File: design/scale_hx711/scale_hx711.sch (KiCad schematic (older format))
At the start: 0 parts

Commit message: PCB Files added, for scale_hx711
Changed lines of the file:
@@
 F0 "nRF" 50
 F1 "nRF.sch" 50
+F2 "VBAT" O R 6450 3700 50
+F3 "HX711_DATA" I R 6450 4100 50
+F4 "HX711_RATE" O R 6450 4510 50
+F5 "HX711_CLK" B R 6450 4900 50
+F6 "BOOST_EN" O R 6450 5300 50
+F7 "10V_LDO_EN" O R 6450 2900 50
+F8 "Vlc" I R 6450 3300 50
+F9 "EINK_SDIO" O L 4400 3300 50
+F10 "EINK_SCLK" O L 4400 3700 50
+F11 "EINK_CS" O L 4400 4100 50
+F12 "EINK_RST" O L 4400 4510 50
+F13 "EINK_BUSY" I L 4400 4900 50
 $EndSheet
 $Sheet
@@
 F0 "Sheet5E60241E" 50
 F1 "epaper.sch" 50
+F2 "EINK_SDIO" I R 3800 3300 50
+F3 "EINK_SCLK" I R 3800 3700 50
+F4 "EINK_CS" I R 3800 4100 50
+F5 "EINK_RST" I R 3800 4510 50
+F6 "EINK_BUSY" O R 3800 4900 50
 $EndSheet
 $Sheet
@@
 F0 "Sheet5E602498" 50
 F1 "loadcell.sch" 50
+F2 "VBAT" I L 8550 3700 50
+F3 "HX711_RATE" I L 8550 4510 50
+F4 "HX711_DATA" O L 8550 4100 50
+F5 "HX711_CLK" B L 8550 4900 50
+F6 "BOOST_EN" I L 8550 5300 50
+F7 "10V_LDO_EN" I L 8550 2900 50
+F8 "Vlc" O L 8550 3300 50
 $EndSheet
+Wire Wire Line
+	3800 3300 4400 3300
+Wire Wire Line
+	4400 3700 3800 3700
+Wire Wire Line
+	3800 4100 4400 4100
+Wire Wire Line
+	3800 4510 4400 4510
+Wire Wire Line
+	4400 4900 3800 4900
+Wire Wire Line
+	6450 5300 8550 5300
+Wire Wire Line
+	8550 4900 6450 4900
+Wire Wire Line
+	6450 4510 8550 4510
+Wire Wire Line
+	8550 4100 6450 4100
+Wire Wire Line
+	6450 3700 8550 3700
+Wire Wire Line
+	8550 3300 6450 3300
+Wire Wire Line
+	6450 2900 8550 2900
 $EndSCHEMATC

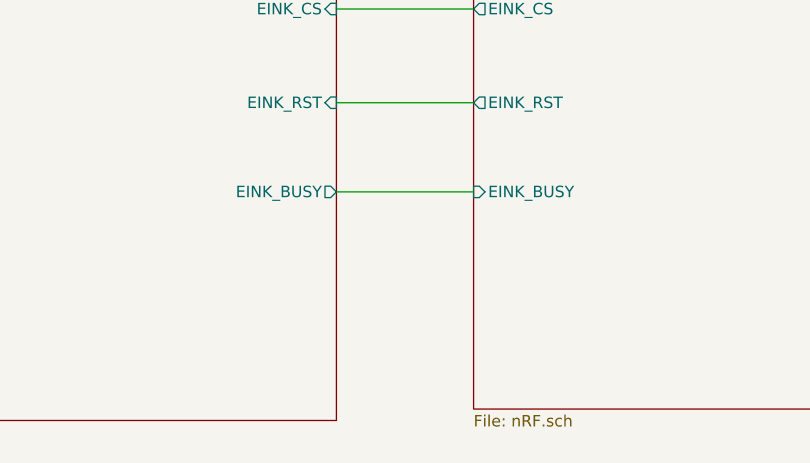
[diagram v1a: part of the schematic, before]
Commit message: DC, CS pins separated, issue fixed. In both scale_hx711 and scale_ltc6915.
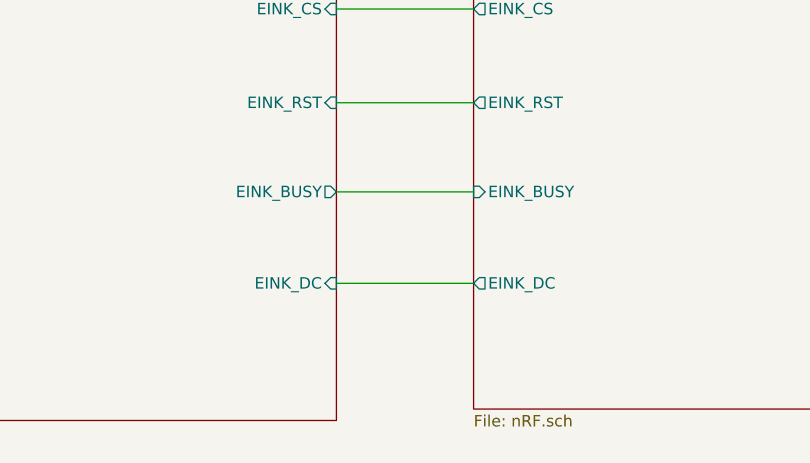
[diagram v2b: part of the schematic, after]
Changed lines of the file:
@@
 F12 "EINK_RST" O L 4400 4510 50
 F13 "EINK_BUSY" I L 4400 4900 50
+F14 "EINK_DC" O L 4400 5300 50
 $EndSheet
 $Sheet
@@
 F5 "EINK_RST" I R 3800 4510 50
 F6 "EINK_BUSY" O R 3800 4900 50
+F7 "EINK_DC" I R 3800 5300 50
 $EndSheet
 $Sheet
@@
 Wire Wire Line
 	6450 2900 8550 2900
+Wire Wire Line
+	3800 5300 4400 5300
 $EndSCHEMATC
